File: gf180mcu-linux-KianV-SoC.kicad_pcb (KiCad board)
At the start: 4 copper layers, 94.7 x 52 mm, 65 parts, among them CN1 HC-PBB40C-70DS-0.4V-2.0-02_CU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, J1 Micro_SD_Card, J2 Conn_01x06_Pin, J3 Conn_01x06_Pin, J4 Conn_02x06_Top_Bottom_custom, J5 USB_C_Receptacle_PowerOnly_6P, SW1 SW_Push, U1 MT48LC16M16A2P, U2 TPS3808DBV, U3 TLV62569DBV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

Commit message: more comments
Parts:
- moved C16 3.13 mm to (160.7, 207.9), turned to -90 degrees
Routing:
- net /3V3: track 483.8 -> 489.9 mm
- net GND: track 60.0 -> 59.0 mm, vias 208 -> 215
- net /UART_TX: track 34.1 -> 33.5 mm

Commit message: kicad: fix capacitor footprints + add GND stitching vias
Switch C1/C3/C28 from resistor footprints to proper 0603 capacitor footprints (C1 to JLCPCB lib + 3D model)

Tweak pad sizes/placement + silkscreen/ref visibility

Add additional GND vias for stitching and minor route/via coordinate cleanup
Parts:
- C1: footprint Resistor_SMD:R_0603_1608Metric -> PCM_JLCPCB:C_0603
- C28, C3: footprint Resistor_SMD:R_0603_1608Metric -> Capacitor_SMD:C_0603_1608Metric
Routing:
- net GND: vias 215 -> 280

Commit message: andrew's small tweaks
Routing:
- net /SDRAM_D12: track 29.5 -> 30.1 mm
- net /SDRAM_D11: track 33.1 -> 33.6 mm
- net GND: vias 280 -> 279

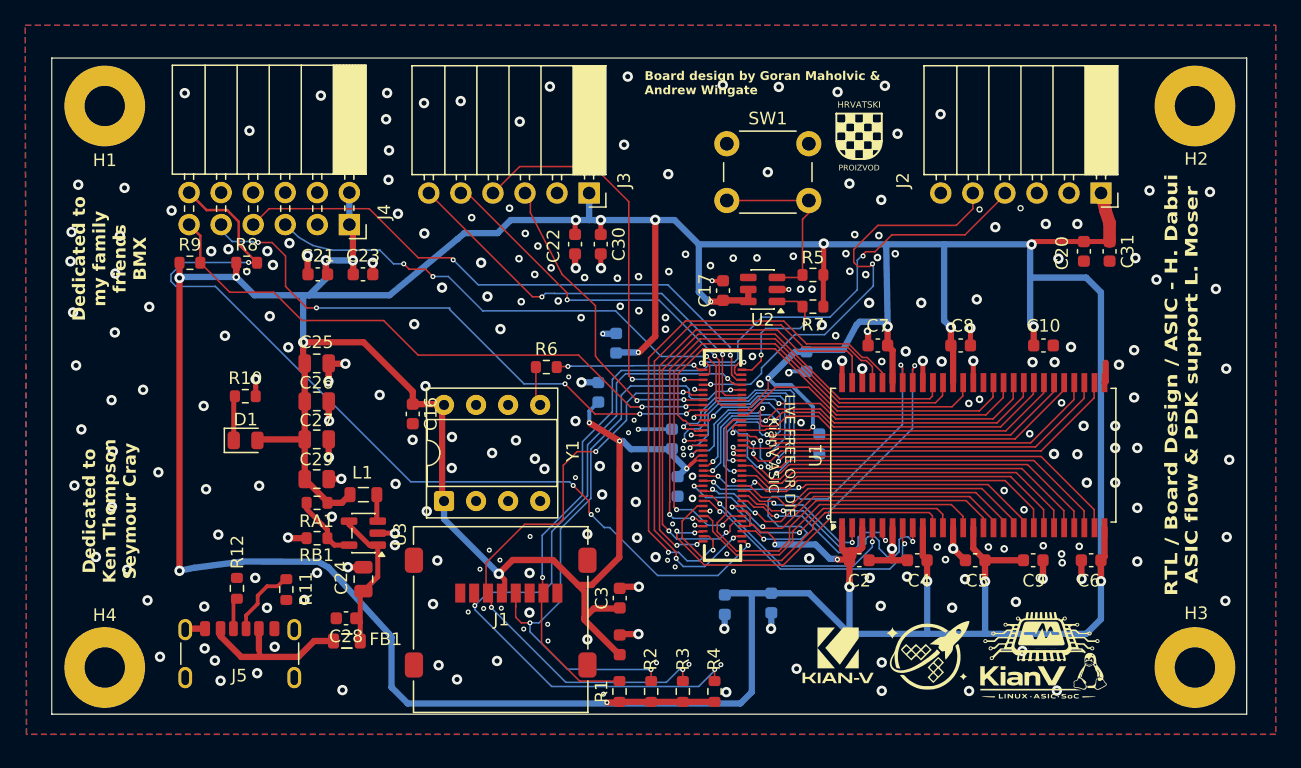
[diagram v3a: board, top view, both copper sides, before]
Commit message: pcb: DFM cleanup, SD card footprint update, oscillator fixes
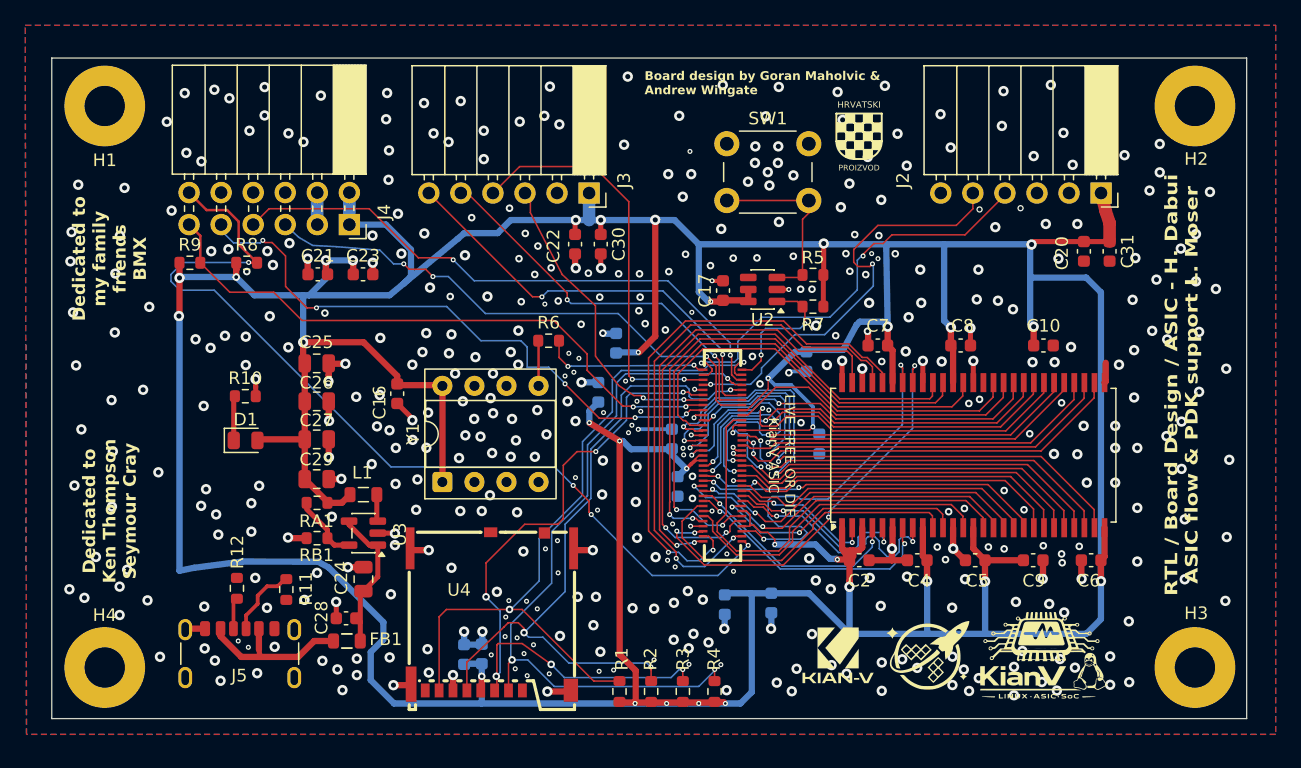
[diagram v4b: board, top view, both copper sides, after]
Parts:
- removed J1: Micro_SD_Card, Connector_Card:microSD_HC_Molex_47219-2001
- added U4: 503398-1892, footprint:TF-SMD_503398-1892, F.Cu at (167.0, 223.6)
- C1, C3: moved to B.Cu
- moved C1 12.4 mm to (164.8, 227.0)
- moved C3 11.8 mm to (166.2, 226.9)
- moved R6 2.10 mm to (171.5, 202.1)
- moved C16 2.02 mm to (159.5, 206.3)
- moved Y1 1.52 mm to (163.1, 213.3)
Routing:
- net GND: track 59.0 -> 73.5 mm, vias 279 -> 461
- net /SPI0_MISO: track 43.4 -> 57.2 mm
- net /SPI0_MOSI: track 48.5 -> 56.7 mm, vias 4 -> 6
- net /3V3: track 489.9 -> 482.8 mm, vias 29 -> 32
- net /SPI0_SCLK: track 48.1 -> 53.8 mm
- net /SPI0_CSN: track 59.8 -> 57.1 mm
- net /clk: track 11.7 -> 13.2 mm
- net /SPI1_MOSI: track 45.9 -> 47.3 mm
- net Net-(Y1-OUT): track 2.66 -> 3.56 mm
- net /SPI1_CSN: track 48.0 -> 48.8 mm
- net /FLASH_MOSI: track 31.2 -> 30.7 mm
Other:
- board size 94.7 x 52 mm -> 94.7 x 52.4 mm

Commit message: update connector assigments and reroute
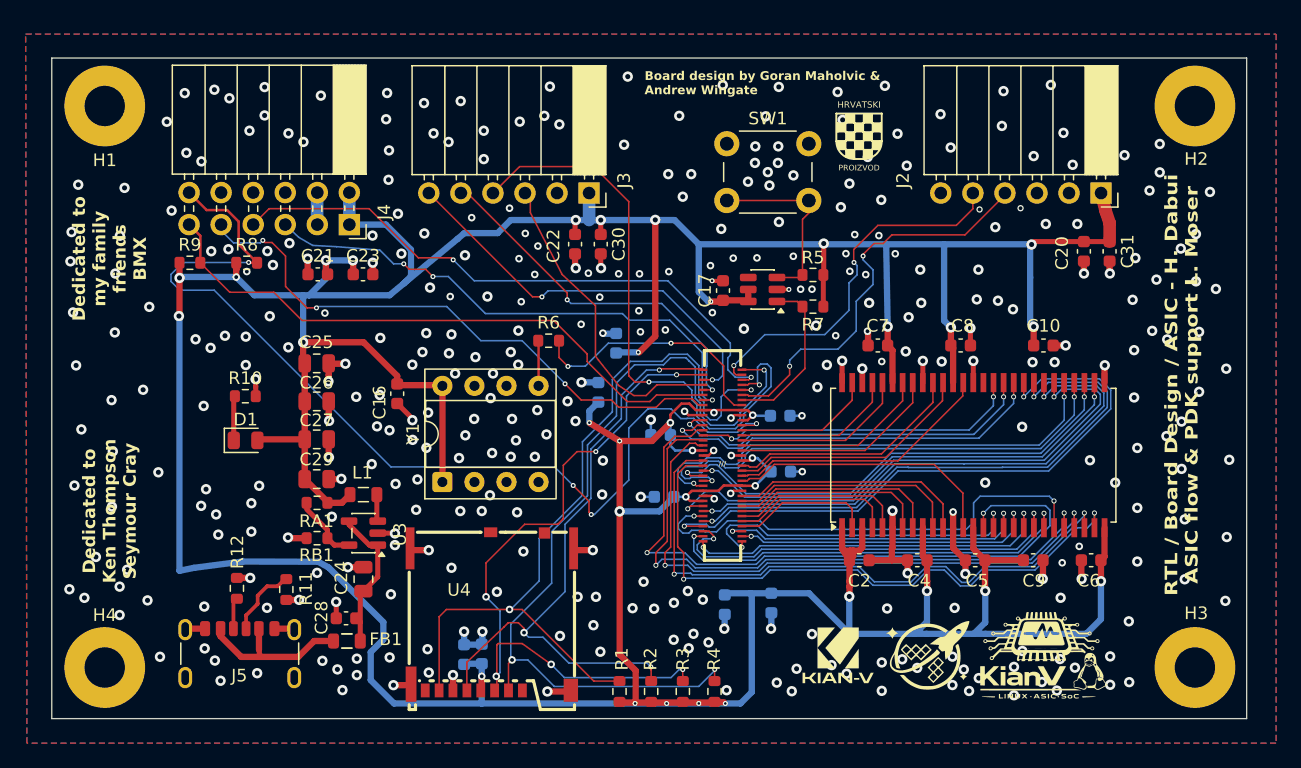
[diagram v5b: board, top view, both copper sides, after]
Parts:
- CN1: value HC-PBB40C-70DS-0.4V-2.0-02_CUSTOM -> Conn_02x35_Counter_Clockwise; footprint C19089262:CONN-SMD_70P-P0.40_HC-PBB40C-70DS-0.4V-3.0-02 -> LD-CONNECTORS:CONN-SMD_70P-P0.40_HC-PBB40C-70DS-0.4V-3.0-02
- moved C18 15.6 mm to (180.6, 214.5), turned to 180 degrees
- moved C12 8.26 mm to (189.9, 212.5), turned to 0 degrees
- moved C19 3.82 mm to (189.8, 208.1), turned to 0 degrees
- moved C13 0.95 mm to (180.4, 209.6), turned to 180 degrees
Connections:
- CN1 pad 1: /clk -> /SPI0_SCLK
- CN1 pad 10: /SPI0_SCLK -> GND
- CN1 pad 11: /SPI0_MOSI -> /SDRAM_CLK
- CN1 pad 12: /FLASH_CSN -> /SDRAM_CKE
- CN1 pad 13: /FLASH_SCLK -> /SDRAM_DQM0
- CN1 pad 14: /FLASH_MOSI -> /SDRAM_DQM1
- CN1 pad 15: /SPI1_CSN -> /SDRAM_A0
- CN1 pad 16: /SPI1_SCLK -> /SDRAM_A1
- CN1 pad 17: /SPI1_MOSI -> /3V3
- CN1 pad 18: /3V3 -> GND
- CN1 pad 19: GND -> /SDRAM_A2
- CN1 pad 2: /rst_n -> /SPI0_MOSI
- CN1 pad 20: /SDRAM_CLK -> /SDRAM_A3
- CN1 pad 21: /SDRAM_CKE -> /SDRAM_A4
- CN1 pad 22: /SDRAM_DQM0 -> /SDRAM_A5
- CN1 pad 23: /SDRAM_DQM1 -> /SDRAM_A6
- CN1 pad 24: /SDRAM_A0 -> /SDRAM_A7
- CN1 pad 25: /SDRAM_A1 -> /3V3
- CN1 pad 26: /3V3 -> GND
- CN1 pad 27: GND -> /3V3
- CN1 pad 28: /SDRAM_A2 -> /SDRAM_A8
- CN1 pad 29: /SDRAM_A3 -> /SDRAM_A9
- CN1 pad 3: /UART_RX -> /FLASH_CSN
- CN1 pad 30: /SDRAM_A4 -> /SDRAM_A10
- CN1 pad 31: /SDRAM_A5 -> /SDRAM_A11
- CN1 pad 32: /SDRAM_A6 -> /SDRAM_A12
- CN1 pad 33: /SDRAM_A7 -> /SDRAM_BA0
- CN1 pad 34: GND -> /SDRAM_BA1
- CN1 pad 35: /3V3 -> /SDRAM_nCS
- CN1 pad 36: GND -> /SDRAM_nWE
- CN1 pad 37: /3V3 -> /SDRAM_nRAS
- CN1 pad 38: /SDRAM_A8 -> /SDRAM_nCAS
- CN1 pad 39: /SDRAM_A9 -> /SDRAM_D0
- CN1 pad 4: /SPI0_MISO -> /FLASH_SCLK
- CN1 pad 40: /SDRAM_A10 -> /SDRAM_D1
- CN1 pad 41: /SDRAM_A11 -> /SDRAM_D2
- CN1 pad 42: /SDRAM_A12 -> /SDRAM_D3
- CN1 pad 43: /SDRAM_BA0 -> /SDRAM_D4
- CN1 pad 44: /SDRAM_BA1 -> /SDRAM_D5
- CN1 pad 45: /SDRAM_nCS -> /SDRAM_D6
- CN1 pad 47: /SDRAM_nWE -> /3V3
- CN1 pad 48: /SDRAM_nRAS -> /SDRAM_D7
- CN1 pad 49: /SDRAM_nCAS -> /SDRAM_D8
- CN1 pad 5: /FLASH_MISO -> /FLASH_MOSI
- CN1 pad 50: /SDRAM_D0 -> /SDRAM_D9
- CN1 pad 51: /SDRAM_D1 -> /SDRAM_D10
- CN1 pad 52: /SDRAM_D2 -> /3V3
- CN1 pad 53: /SDRAM_D3 -> GND
- CN1 pad 54: /SDRAM_D4 -> /SDRAM_D11
- CN1 pad 55: /SDRAM_D5 -> /SDRAM_D12
- CN1 pad 56: /SDRAM_D6 -> /SDRAM_D13
- CN1 pad 57: GND -> /SDRAM_D14
- CN1 pad 58: /3V3 -> /SDRAM_D15
- CN1 pad 59: /SDRAM_D7 -> /GPIO0
- CN1 pad 6: /SPI1_MISO -> /SPI1_CSN
- CN1 pad 60: /SDRAM_D8 -> /3V3
- CN1 pad 61: /SDRAM_D9 -> GND
- CN1 pad 62: /SDRAM_D10 -> /3V3
- CN1 pad 63: GND -> /clk
- CN1 pad 64: /3V3 -> /rst_n
- CN1 pad 65: /SDRAM_D11 -> /UART_RX
- CN1 pad 66: /SDRAM_D12 -> /SPI0_MISO
- CN1 pad 67: /SDRAM_D13 -> /FLASH_MISO
- CN1 pad 68: /SDRAM_D14 -> /SPI1_MISO
- CN1 pad 69: /SDRAM_D15 -> /UART_TX
- CN1 pad 7: /UART_TX -> /SPI1_SCLK
- CN1 pad 70: /GPIO0 -> /SPI0_CSN
- CN1 pad 8: /SPI0_CSN -> /SPI1_MOSI
- CN1 pad 9: GND -> /3V3
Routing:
- net /3V3: track 482.8 -> 442.8 mm, vias 32 -> 35
- net /SDRAM_D14: track 44.0 -> 13.0 mm, vias 2 -> 0
- net /SDRAM_D13: track 44.1 -> 14.0 mm, vias 2 -> 0
- net /SDRAM_D10: track 45.5 -> 18.9 mm, vias 2 -> 0
- net /SDRAM_D15: track 36.4 -> 11.1 mm, vias 2 -> 0
- net /SDRAM_D8: track 44.2 -> 21.0 mm, vias 2 -> 0
- net /SDRAM_D9: track 40.2 -> 19.5 mm, vias 2 -> 0
- net /SDRAM_DQM0: track 35.1 -> 54.2 mm, vias 0 -> 2
- net /SDRAM_A12: track 31.4 -> 49.8 mm
- net /SDRAM_D11: track 33.6 -> 16.7 mm, vias 4 -> 0
- net /SDRAM_A2: track 32.2 -> 48.7 mm
- net /SDRAM_A0: track 33.4 -> 49.3 mm
- net /FLASH_MISO: track 32.6 -> 48.0 mm
- net /SDRAM_D12: track 30.1 -> 15.6 mm, vias 2 -> 0
- net /SDRAM_A11: track 32.5 -> 44.8 mm
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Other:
- board text added: "///"
- board text removed: "LIVE FREE OR DIE KianV ASIC"
